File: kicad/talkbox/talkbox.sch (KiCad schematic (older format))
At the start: 43 parts, among them J1 AudioJack2, J2 Barrel_Jack_Switch, J3 Conn_02x04_Odd_Even, J4 AudioJack2, SW1 SW_SPST, U1 TL071, U2 logo, U3 LT1054xSOIC16, U4 SW_3PDT, U5 LM7812_TO220, U6 LM7912_TO220

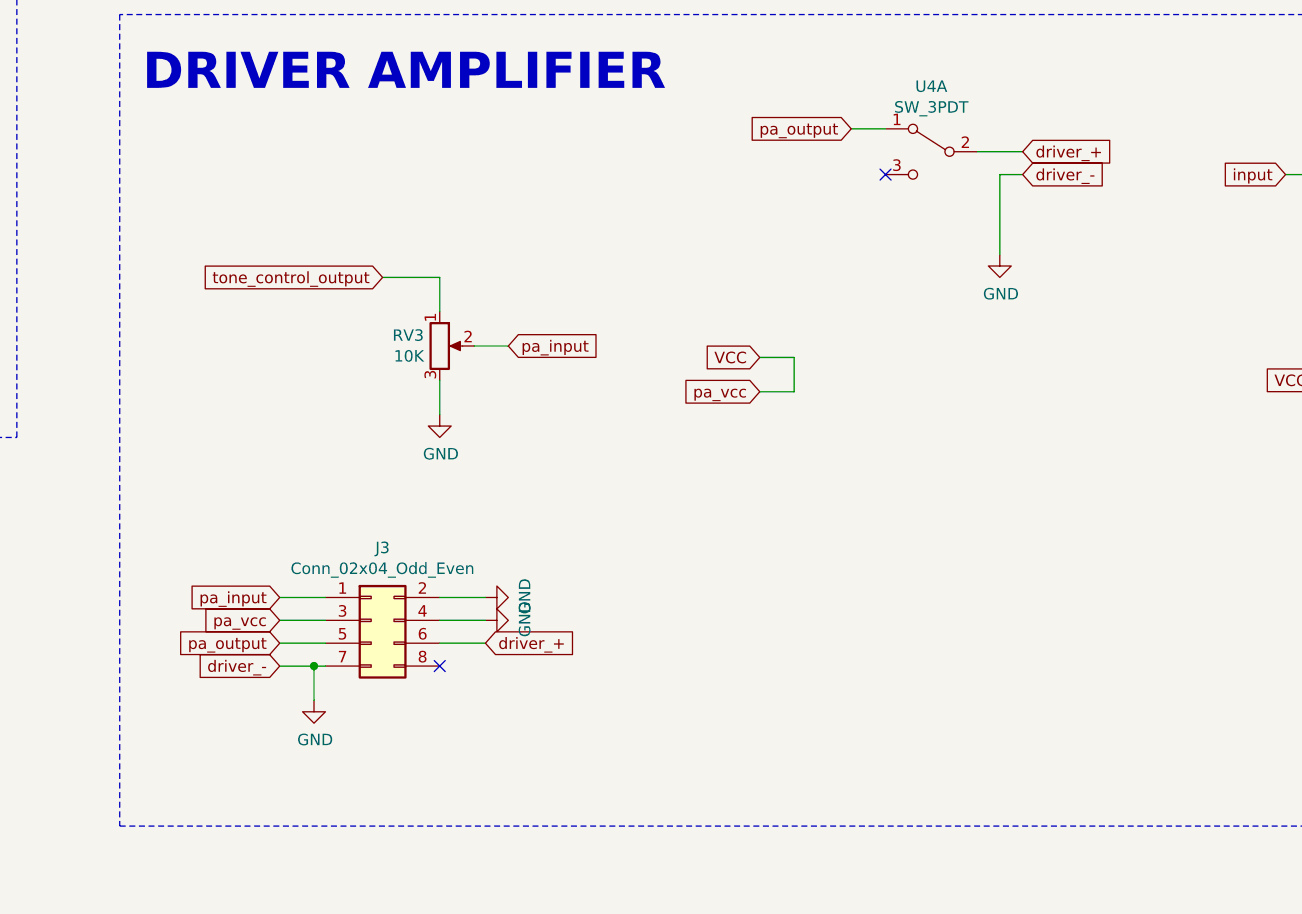
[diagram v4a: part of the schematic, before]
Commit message: Re-labeled drive- to GND
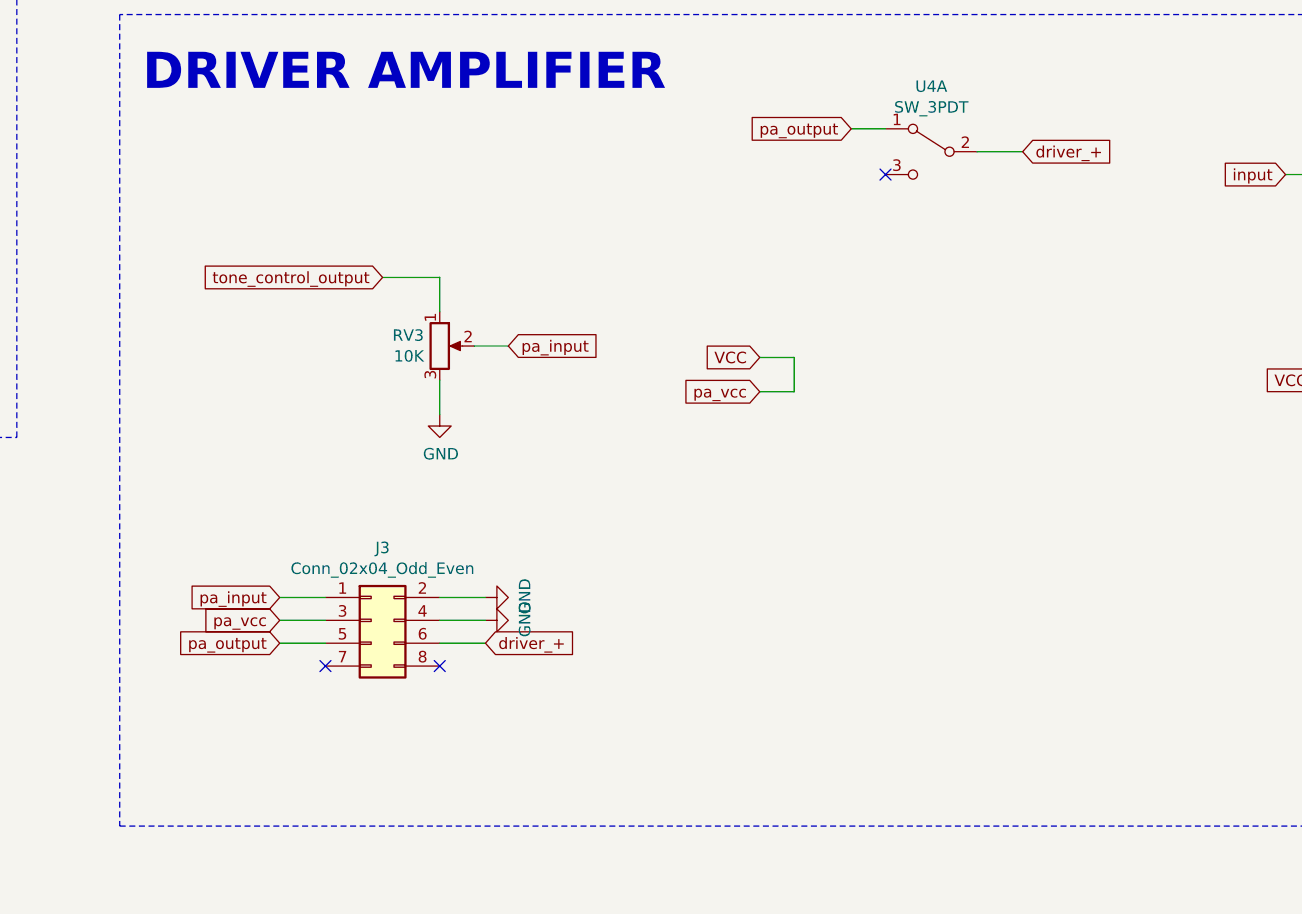
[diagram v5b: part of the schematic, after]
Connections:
- net GND: no longer J3.7 (Pin_7)
- no-connect marks 7 -> 8
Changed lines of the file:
@@
 Wire Notes Line width 39 style dash_dot rgb(132, 132, 132)
 	14750 8750 14800 5200
-$Comp
-L power:GND #PWR09
-U 1 1 5F3250F6
-P 9550 6950
-F 0 "#PWR09" H 9550 6700 50  0001 C CNN
-F 1 "GND" H 9555 6777 50  0000 C CNN
-F 2 "" H 9550 6950 50  0001 C CNN
-F 3 "" H 9550 6950 50  0001 C CNN
-	1    9550 6950
-	1    0    0    -1
-$EndComp
 Wire Wire Line
 	9550 6800 9550 6950
@@
 F 3 "" H 11200 3550 50  0001 C CNN
 	1    11100 3650
-	1    0    0    -1
-$EndComp
-$Comp
-L power:GND #PWR013
-U 1 1 5ED9C4F9
-P 12000 6250
-F 0 "#PWR013" H 12000 6000 50  0001 C CNN
-F 1 "GND" H 12005 6077 50  0000 C CNN
-F 2 "" H 12000 6250 50  0001 C CNN
-F 3 "" H 12000 6250 50  0001 C CNN
-	1    12000 6250
 	1    0    0    -1
 $EndComp
@@
 	11900 5800 12100 5800
 Wire Wire Line
-	12100 5900 12000 5900
-Wire Wire Line
 	11350 5700 11500 5700
-Wire Wire Line
-	12000 5900 12000 6250
 Wire Wire Line
 	13250 5900 13400 5900
@@
 Text GLabel 8850 7850 0    50   Input ~ 0
 pa_vcc
-Wire Wire Line
-	8850 8050 9000 8050
-Text GLabel 8850 8050 0    50   Input ~ 0
-driver_-
 Text GLabel 12100 5800 2    50   Input ~ 0
 driver_+
-Text GLabel 12100 5900 2    50   Input ~ 0
-driver_-
 $Comp
 L Device:CP C2
@@
 	0    -1   -1   0
 $EndComp
-$Comp
-L power:GND #PWR0103
-U 1 1 5EDE914A
-P 9000 8200
-F 0 "#PWR0103" H 9000 7950 50  0001 C CNN
-F 1 "GND" H 9005 8027 50  0000 C CNN
-F 2 "" H 9000 8200 50  0001 C CNN
-F 3 "" H 9000 8200 50  0001 C CNN
-	1    9000 8200
-	1    0    0    -1
-$EndComp
-Wire Wire Line
-	9000 8200 9000 8050
-Connection ~ 9000 8050
-Wire Wire Line
-	9000 8050 9050 8050
 Wire Wire Line
 	14850 3050 14850 3150
@@
 Wire Wire Line
 	9800 3350 10700 3350
+$Comp
+L power:GND #PWR09
+U 1 1 5EE63EA4
+P 9550 6950
+F 0 "#PWR09" H 9550 6700 50  0001 C CNN
+F 1 "GND" H 9555 6777 50  0000 C CNN
+F 2 "" H 9550 6950 50  0001 C CNN
+F 3 "" H 9550 6950 50  0001 C CNN
+	1    9550 6950
+	1    0    0    -1
+$EndComp
+NoConn ~ 9050 8050
 $EndSCHEMATC

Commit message: PCB done v1.0. Generated gerbers for fab
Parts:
- C3: value 22pF -> 6.8nF
- C6: value 4.7nF -> 10nF
- C7: value 4.7nF -> 47nF
- R3: value 9.1K -> 47K
- R4: value 9.1K -> 22K
- RV1: value 10K -> 20K
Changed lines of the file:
@@
 P 4350 4800
 F 0 "C3" V 4098 4800 50  0000 C CNN
-F 1 "22pF" V 4189 4800 50  0000 C CNN
+F 1 "6.8nF" V 4189 4800 50  0000 C CNN
 F 2 "Capacitor_SMD:C_0603_1608Metric" H 4388 4650 50  0001 C CNN
 F 3 "~" H 4350 4800 50  0001 C CNN
@@
 P 5200 5300
 F 0 "RV1" H 5131 5346 50  0000 R CNN
-F 1 "10K" H 5131 5255 50  0000 R CNN
+F 1 "20K" H 5131 5255 50  0000 R CNN
 F 2 "Potentiometer_THT:Potentiometer_Alps_RK09K_Single_Vertical" H 5200 5300 50  0001 C CNN
 F 3 "~" H 5200 5300 50  0001 C CNN
@@
 P 4350 5800
 F 0 "R3" H 4420 5846 50  0000 L CNN
-F 1 "9.1K" H 4420 5755 50  0000 L CNN
+F 1 "47K" H 4420 5755 50  0000 L CNN
 F 2 "Resistor_SMD:R_0603_1608Metric" V 4280 5800 50  0001 C CNN
 F 3 "~" H 4350 5800 50  0001 C CNN
@@
 P 5200 4450
 F 0 "R4" H 5270 4496 50  0000 L CNN
-F 1 "9.1K" H 5270 4405 50  0000 L CNN
+F 1 "22K" H 5270 4405 50  0000 L CNN
 F 2 "Resistor_SMD:R_0603_1608Metric" V 5130 4450 50  0001 C CNN
 F 3 "~" H 5200 4450 50  0001 C CNN
@@
 P 5200 6150
 F 0 "C6" V 4948 6150 50  0000 C CNN
-F 1 "4.7nF" V 5039 6150 50  0000 C CNN
+F 1 "10nF" V 5039 6150 50  0000 C CNN
 F 2 "Capacitor_SMD:C_0603_1608Metric" H 5238 6000 50  0001 C CNN
 F 3 "~" H 5200 6150 50  0001 C CNN
@@
 P 5850 5300
 F 0 "C7" V 5598 5300 50  0000 C CNN
-F 1 "4.7nF" V 5689 5300 50  0000 C CNN
+F 1 "47nF" V 5689 5300 50  0000 C CNN
 F 2 "Capacitor_SMD:C_0603_1608Metric" H 5888 5150 50  0001 C CNN
 F 3 "~" H 5850 5300 50  0001 C CNN

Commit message: Added partially mouser part numbers
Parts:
- C1, C2, C9: Mouser part (none) -> 598-AVE106M35C12T-F
- C10: Mouser part (none) -> 603-CC603KRX7R9BB202
- C11, C4, C5: Mouser part (none) -> 661-EMZJ6R3A101ME61G
- C12, C13, C8: Mouser part (none) -> 555-RVS-50V2R2MU-R
- C14, C15: Mouser part (none) -> 555-RVS-50VR47MU-R
- C6: Mouser part (none) -> 710-885012206040
- C7: Mouser part (none) -> 140-VE470M1CTR0505
- D1, D2: Mouser part (none) -> 327-BR1101WTR
- J1, J4: Mouser part (none) -> 550-10284G
- J2: Mouser part (none) -> 490-PJ-102BH
- R4, R5: Mouser part (none) -> 71-CRCW060322K0FKEAC
- R6: Mouser part (none) -> 652-CR0603FX-2403ELF
- R7, R8: Mouser part (none) -> 71-CRCW0603470RFKEAC
- RV1, RV2: Mouser part (none) -> 652-PTV09A-4030UB203
- RV3: Mouser part (none) -> 688-RK09D113000Q
- SW1: Mouser part (none) -> 611-OS102011MA1QN1
- U3: Mouser part (none) -> 595-LT1054CDWR
- U4: Mouser part (none) -> 474-COM-15133
- U5: Mouser part (none) -> 511-L78M12CDT-TR
- U6: Mouser part (none) -> 512-KA79M12RTF
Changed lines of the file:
@@
 F 2 "Button_Switch_THT:SW_CuK_OS102011MA1QN1_SPDT_Angled" H 9350 3350 50  0001 C CNN
 F 3 "~" H 9350 3350 50  0001 C CNN
+F 4 "611-OS102011MA1QN1" H 9350 3350 50  0001 C CNN "Mouser part"
 	1    9350 3350
 	1    0    0    -1
@@
 F 2 "Connector_BarrelJack:BarrelJack_CUI_PJ-102AH_Horizontal" H 8600 3410 50  0001 C CNN
 F 3 "~" H 8600 3410 50  0001 C CNN
+F 4 "490-PJ-102BH " H 8550 3450 50  0001 C CNN "Mouser part"
 	1    8550 3450
 	1    0    0    -1
@@
 F 2 "Resistor_SMD:R_0603_1608Metric" V 14780 2500 50  0001 C CNN
 F 3 "~" H 14850 2500 50  0001 C CNN
+F 4 "71-CRCW0603470RFKEAC" H 14850 2500 50  0001 C CNN "Mouser part"
 	1    14850 2500
 	-1   0    0    1
@@
 F 2 "LED_SMD:LED_1206_3216Metric" H 14850 2900 50  0001 C CNN
 F 3 "~" H 14850 2900 50  0001 C CNN
+F 4 "327-BR1101WTR" H 14850 2900 50  0001 C CNN "Mouser part"
 	1    14850 2900
 	0    -1   -1   0
@@
 F 2 "Capacitor_SMD:C_0603_1608Metric" H 12488 3500 50  0001 C CNN
 F 3 "~" H 12450 3650 50  0001 C CNN
+F 4 "603-CC603KRX7R9BB202" H 12450 3650 50  0001 C CNN "Mouser part"
 	1    12450 3650
 	1    0    0    -1
@@
 F 2 "Resistor_SMD:R_0603_1608Metric" V 11980 3650 50  0001 C CNN
 F 3 "~" H 12050 3650 50  0001 C CNN
+F 4 "652-CR0603FX-2403ELF" H 12050 3650 50  0001 C CNN "Mouser part"
 	1    12050 3650
 	-1   0    0    1
@@
 F 2 "Resistor_SMD:R_0603_1608Metric" V 10330 3850 50  0001 C CNN
 F 3 "~" H 10400 3850 50  0001 C CNN
+F 4 "71-CRCW060322K0FKEAC" H 10400 3850 50  0001 C CNN "Mouser part"
 	1    10400 3850
 	0    -1   -1   0
@@
 F 2 "Capacitor_SMD:CP_Elec_5x5.3" H 14438 3450 50  0001 C CNN
 F 3 "~" H 14400 3600 50  0001 C CNN
+F 4 "555-RVS-50VR47MU-R " H 14400 3600 50  0001 C CNN "Mouser part"
 	1    14400 3600
 	-1   0    0    1
@@
 F 2 "Capacitor_SMD:CP_Elec_5x5.3" H 13488 3450 50  0001 C CNN
 F 3 "~" H 13450 3600 50  0001 C CNN
+F 4 "555-RVS-50V2R2MU-R" H 13450 3600 50  0001 C CNN "Mouser part"
 	1    13450 3600
 	-1   0    0    1
@@
 F 2 "Capacitor_SMD:CP_Elec_5x5.3" H 14438 2250 50  0001 C CNN
 F 3 "~" H 14400 2400 50  0001 C CNN
+F 4 "555-RVS-50VR47MU-R " H 14400 2400 50  0001 C CNN "Mouser part"
 	1    14400 2400
 	1    0    0    -1
@@
 F 2 "Capacitor_SMD:CP_Elec_5x5.3" H 13488 2250 50  0001 C CNN
 F 3 "~" H 13450 2400 50  0001 C CNN
+F 4 "555-RVS-50V2R2MU-R" H 13450 2400 50  0001 C CNN "Mouser part"
 	1    13450 2400
 	1    0    0    -1
@@
 F 2 "Package_TO_SOT_SMD:ATPAK-2" H 13900 2425 50  0001 C CIN
 F 3 "http://www.fairchildsemi.com/ds/LM/LM7805.pdf" H 13900 2150 50  0001 C CNN
+F 4 "511-L78M12CDT-TR " H 13900 2200 50  0001 C CNN "Mouser part"
 	1    13900 2200
 	1    0    0    -1
@@
 F 2 "Package_TO_SOT_SMD:ATPAK-2" H 13900 3150 50  0001 C CIN
 F 3 "http://www.fairchildsemi.com/ds/LM/LM7905.pdf" H 13900 3350 50  0001 C CNN
+F 4 "512-KA79M12RTF " H 13900 3350 50  0001 C CNN "Mouser part"
 	1    13900 3350
 	1    0    0    1
@@
 F 2 "Capacitor_SMD:CP_Elec_5x5.3" H 12888 3500 50  0001 C CNN
 F 3 "~" H 12850 3650 50  0001 C CNN
+F 4 "661-EMZJ6R3A101ME61G" H 12850 3650 50  0001 C CNN "Mouser part"
 	1    12850 3650
 	-1   0    0    1
@@
 F 2 "Capacitor_SMD:CP_Elec_5x5.3" H 11688 3600 50  0001 C CNN
 F 3 "~" H 11650 3750 50  0001 C CNN
+F 4 "598-AVE106M35C12T-F" H 11650 3750 50  0001 C CNN "Mouser part"
 	1    11650 3750
 	1    0    0    -1
@@
 F 2 "Capacitor_SMD:CP_Elec_5x5.3" H 9838 3450 50  0001 C CNN
 F 3 "~" H 9800 3600 50  0001 C CNN
+F 4 "555-RVS-50V2R2MU-R" H 9800 3600 50  0001 C CNN "Mouser part"
 	1    9800 3600
 	1    0    0    -1
@@
 F 2 "Connector_Audio_Extended:Jack_6.35mm_Neutrik_NRJ4HF-1_Horizontal" H 1950 3100 50  0001 C CNN
 F 3 "~" H 1950 3100 50  0001 C CNN
+F 4 "550-10284G " H 1950 3100 50  0001 C CNN "Mouser part"
 	1    1950 3100
 	1    0    0    1
@@
 F 2 "Connector_Audio_Extended:Jack_6.35mm_Neutrik_NRJ4HF-1_Horizontal" H 14150 5800 50  0001 C CNN
 F 3 "~" H 14150 5800 50  0001 C CNN
+F 4 "550-10284G " H 14150 5800 50  0001 C CNN "Mouser part"
 	1    14150 5800
 	-1   0    0    1
@@
 F 2 "LED_SMD:LED_1206_3216Metric" H 14150 7550 50  0001 C CNN
 F 3 "~" H 14150 7550 50  0001 C CNN
+F 4 "327-BR1101WTR" H 14150 7550 50  0001 C CNN "Mouser part"
 	1    14150 7550
 	0    -1   -1   0
@@
 F 2 "Resistor_SMD:R_0603_1608Metric" V 14080 7250 50  0001 C CNN
 F 3 "~" H 14150 7250 50  0001 C CNN
+F 4 "71-CRCW0603470RFKEAC" H 14150 7250 50  0001 C CNN "Mouser part"
 	1    14150 7250
 	-1   0    0    1
@@
 F 2 "Capacitor_SMD:C_0603_1608Metric" H 4388 4650 50  0001 C CNN
 F 3 "~" H 4350 4800 50  0001 C CNN
+F 4 "" V 4350 4800 50  0001 C CNN "Mouser part"
 	1    4350 4800
 	0    -1   -1   0
@@
 F 2 "Capacitor_SMD:CP_Elec_5x5.3" H 4738 3250 50  0001 C CNN
 F 3 "~" H 4700 3400 50  0001 C CNN
+F 4 "661-EMZJ6R3A101ME61G" H 4700 3400 50  0001 C CNN "Mouser part"
 	1    4700 3400
 	0    1    1    0
@@
 F 2 "Package_SO:SOIC-16W_7.5x10.3mm_P1.27mm" H 11200 3550 50  0001 C CNN
 F 3 "" H 11200 3550 50  0001 C CNN
+F 4 "595-LT1054CDWR " H 11100 3650 50  0001 C CNN "Mouser part"
 	1    11100 3650
 	1    0    0    -1
@@
 F 2 "Connector_PinHeader_2.54mm:PinHeader_2x05_P2.54mm_Vertical" H 11600 6100 50  0001 C CNN
 F 3 "" H 11600 6100 50  0001 C CNN
+F 4 " 474-COM-15133" H 11600 6050 50  0001 C CNN "Mouser part"
 	1    11600 6050
 	-1   0    0    -1
@@
 F 2 "Connector_PinHeader_2.54mm:PinHeader_2x05_P2.54mm_Vertical" H 13650 7200 50  0001 C CNN
 F 3 "" H 13650 7200 50  0001 C CNN
+F 4 " 474-COM-15133" H 13650 7150 50  0001 C CNN "Mouser part"
 	3    13650 7150
 	-1   0    0    -1
@@
 F 2 "Connector_PinHeader_2.54mm:PinHeader_2x05_P2.54mm_Vertical" H 13500 6100 50  0001 C CNN
 F 3 "" H 13500 6100 50  0001 C CNN
+F 4 " 474-COM-15133" H 13500 6050 50  0001 C CNN "Mouser part"
 	2    13500 6050
 	-1   0    0    -1
@@
 F 2 "Potentiometer_THT:Potentiometer_Alps_RK09K_Single_Vertical" H 5400 2250 50  0001 C CNN
 F 3 "~" H 5400 2250 50  0001 C CNN
+F 4 "652-PTV09A-4030UB203 " H 5400 2250 50  0001 C CNN "Mouser part"
 	1    5400 2250
 	0    -1   -1   0
@@
 F 2 "Potentiometer_THT:Potentiometer_Alps_RK09K_Single_Vertical" H 9550 6650 50  0001 C CNN
 F 3 "~" H 9550 6650 50  0001 C CNN
+F 4 "688-RK09D113000Q" H 9550 6650 50  0001 C CNN "Mouser part"
 	1    9550 6650
 	1    0    0    -1
@@
 F 2 "Capacitor_SMD:CP_Elec_5x5.3" H 4738 2500 50  0001 C CNN
 F 3 "~" H 4700 2650 50  0001 C CNN
+F 4 "661-EMZJ6R3A101ME61G" H 4700 2650 50  0001 C CNN "Mouser part"
 	1    4700 2650
 	0    -1   -1   0
@@
 F 2 "Potentiometer_THT:Potentiometer_Alps_RK09K_Single_Vertical" H 5200 5300 50  0001 C CNN
 F 3 "~" H 5200 5300 50  0001 C CNN
+F 4 "652-PTV09A-4030UB203 " H 5200 5300 50  0001 C CNN "Mouser part"
 	1    5200 5300
 	1    0    0    -1
@@
 F 2 "Resistor_SMD:R_0603_1608Metric" V 5130 4450 50  0001 C CNN
 F 3 "~" H 5200 4450 50  0001 C CNN
+F 4 "71-CRCW060322K0FKEAC" H 5200 4450 50  0001 C CNN "Mouser part"
 	1    5200 4450
 	-1   0    0    1
@@
 F 2 "Capacitor_SMD:C_0603_1608Metric" H 5238 6000 50  0001 C CNN
 F 3 "~" H 5200 6150 50  0001 C CNN
+F 4 "710-885012206040" H 5200 6150 50  0001 C CNN "Mouser part"
 	1    5200 6150
 	1    0    0    -1
@@
 F 2 "Capacitor_SMD:C_0603_1608Metric" H 5888 5150 50  0001 C CNN
 F 3 "~" H 5850 5300 50  0001 C CNN
+F 4 "140-VE470M1CTR0505" H 5850 5300 50  0001 C CNN "Mouser part"
 	1    5850 5300
 	0    1    1    0
@@
 F 2 "Capacitor_SMD:CP_Elec_5x5.3" H 3138 2950 50  0001 C CNN
 F 3 "~" H 3100 3100 50  0001 C CNN
+F 4 "598-AVE106M35C12T-F" H 3100 3100 50  0001 C CNN "Mouser part"
 	1    3100 3100
 	0    -1   -1   0
@@
 F 2 "Capacitor_SMD:CP_Elec_5x5.3" H 3138 2100 50  0001 C CNN
 F 3 "~" H 3100 2250 50  0001 C CNN
+F 4 "598-AVE106M35C12T-F" H 3100 2250 50  0001 C CNN "Mouser part"
 	1    3100 2250
 	0    1    1    0

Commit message: Finished BOM with mouser part numbers
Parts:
- C12, C13, C8: Mouser part 555-RVS-50V2R2MU-R -> 661-EMVE630ADA3R3ME5
- C14, C15: Mouser part 555-RVS-50VR47MU-R -> RVS-50V010MU-R
- C3: Mouser part (none) -> 710-885012206088
- R1: Mouser part (none) -> 667-ERJ-3GEYJ105V
- R2: Mouser part (none) -> 71-CRCW06032K00FKEAC
- R3: Mouser part (none) -> 71-CRCW060347K0FKEAC
- RV3: Mouser part 688-RK09D113000Q -> 652-PTV09A-4025FB103
- U1: Mouser part (none) -> 511-TL071CDT
- U4: Mouser part 474-COM-15133 -> 612-FS573PLT2B2M1QE
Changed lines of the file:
@@
 F 2 "Capacitor_SMD:CP_Elec_5x5.3" H 14438 3450 50  0001 C CNN
 F 3 "~" H 14400 3600 50  0001 C CNN
-F 4 "555-RVS-50VR47MU-R " H 14400 3600 50  0001 C CNN "Mouser part"
+F 4 "RVS-50V010MU-R" H 14400 3600 50  0001 C CNN "Mouser part"
 	1    14400 3600
 	-1   0    0    1
@@
 F 2 "Capacitor_SMD:CP_Elec_5x5.3" H 13488 3450 50  0001 C CNN
 F 3 "~" H 13450 3600 50  0001 C CNN
-F 4 "555-RVS-50V2R2MU-R" H 13450 3600 50  0001 C CNN "Mouser part"
+F 4 "661-EMVE630ADA3R3ME5 " H 13450 3600 50  0001 C CNN "Mouser part"
 	1    13450 3600
 	-1   0    0    1
@@
 F 2 "Capacitor_SMD:CP_Elec_5x5.3" H 14438 2250 50  0001 C CNN
 F 3 "~" H 14400 2400 50  0001 C CNN
-F 4 "555-RVS-50VR47MU-R " H 14400 2400 50  0001 C CNN "Mouser part"
+F 4 "RVS-50V010MU-R" H 14400 2400 50  0001 C CNN "Mouser part"
 	1    14400 2400
 	1    0    0    -1
@@
 F 2 "Capacitor_SMD:CP_Elec_5x5.3" H 13488 2250 50  0001 C CNN
 F 3 "~" H 13450 2400 50  0001 C CNN
-F 4 "555-RVS-50V2R2MU-R" H 13450 2400 50  0001 C CNN "Mouser part"
+F 4 "661-EMVE630ADA3R3ME5 " H 13450 2400 50  0001 C CNN "Mouser part"
 	1    13450 2400
 	1    0    0    -1
@@
 F 2 "Capacitor_SMD:CP_Elec_5x5.3" H 9838 3450 50  0001 C CNN
 F 3 "~" H 9800 3600 50  0001 C CNN
-F 4 "555-RVS-50V2R2MU-R" H 9800 3600 50  0001 C CNN "Mouser part"
+F 4 "661-EMVE630ADA3R3ME5 " H 9800 3600 50  0001 C CNN "Mouser part"
 	1    9800 3600
 	1    0    0    -1
@@
 F 2 "Capacitor_SMD:C_0603_1608Metric" H 4388 4650 50  0001 C CNN
 F 3 "~" H 4350 4800 50  0001 C CNN
-F 4 "" V 4350 4800 50  0001 C CNN "Mouser part"
+F 4 "710-885012206088" V 4350 4800 50  0001 C CNN "Mouser part"
 	1    4350 4800
 	0    -1   -1   0
@@
 F 2 "Connector_PinHeader_2.54mm:PinHeader_2x05_P2.54mm_Vertical" H 11600 6100 50  0001 C CNN
 F 3 "" H 11600 6100 50  0001 C CNN
-F 4 " 474-COM-15133" H 11600 6050 50  0001 C CNN "Mouser part"
+F 4 "612-FS573PLT2B2M1QE " H 11600 6050 50  0001 C CNN "Mouser part"
 	1    11600 6050
 	-1   0    0    -1
@@
 F 2 "Connector_PinHeader_2.54mm:PinHeader_2x05_P2.54mm_Vertical" H 13650 7200 50  0001 C CNN
 F 3 "" H 13650 7200 50  0001 C CNN
-F 4 " 474-COM-15133" H 13650 7150 50  0001 C CNN "Mouser part"
+F 4 "612-FS573PLT2B2M1QE " H 13650 7150 50  0001 C CNN "Mouser part"
 	3    13650 7150
 	-1   0    0    -1
@@
 F 2 "Connector_PinHeader_2.54mm:PinHeader_2x05_P2.54mm_Vertical" H 13500 6100 50  0001 C CNN
 F 3 "" H 13500 6100 50  0001 C CNN
-F 4 " 474-COM-15133" H 13500 6050 50  0001 C CNN "Mouser part"
+F 4 "612-FS573PLT2B2M1QE " H 13500 6050 50  0001 C CNN "Mouser part"
 	2    13500 6050
 	-1   0    0    -1
@@
 F 2 "Potentiometer_THT:Potentiometer_Alps_RK09K_Single_Vertical" H 9550 6650 50  0001 C CNN
 F 3 "~" H 9550 6650 50  0001 C CNN
-F 4 "688-RK09D113000Q" H 9550 6650 50  0001 C CNN "Mouser part"
+F 4 "652-PTV09A-4025FB103" H 9550 6650 50  0001 C CNN "Mouser part"
 	1    9550 6650
 	1    0    0    -1
@@
 F 2 "Resistor_SMD:R_0603_1608Metric" V 3480 3450 50  0001 C CNN
 F 3 "~" H 3550 3450 50  0001 C CNN
+F 4 "667-ERJ-3GEYJ105V" H 3550 3450 50  0001 C CNN "Mouser part"
 	1    3550 3450
 	-1   0    0    1
@@
 F 2 "Resistor_SMD:R_0603_1608Metric" V 3730 2250 50  0001 C CNN
 F 3 "~" H 3800 2250 50  0001 C CNN
+F 4 "71-CRCW06032K00FKEAC" H 3800 2250 50  0001 C CNN "Mouser part"
 	1    3800 2250
 	0    -1   -1   0
@@
 F 2 "Package_SO:SOIC-8_3.9x4.9mm_P1.27mm" H 5000 3050 50  0001 C CNN
 F 3 "http://www.ti.com/lit/ds/symlink/tl071.pdf" H 5100 3150 50  0001 C CNN
+F 4 "511-TL071CDT" H 4950 3000 50  0001 C CNN "Mouser part"
 	1    4950 3000
 	1    0    0    1
@@
 F 2 "Resistor_SMD:R_0603_1608Metric" V 4280 5800 50  0001 C CNN
 F 3 "~" H 4350 5800 50  0001 C CNN
+F 4 "71-CRCW060347K0FKEAC" H 4350 5800 50  0001 C CNN "Mouser part"
 	1    4350 5800
 	0    1    1    0
